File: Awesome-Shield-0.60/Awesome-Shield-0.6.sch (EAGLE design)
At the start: 22 parts, among them SW1 SPST_TACT-EVQQ2, SW2 DPDT, U1 LIGHTSENSORTEMT6000

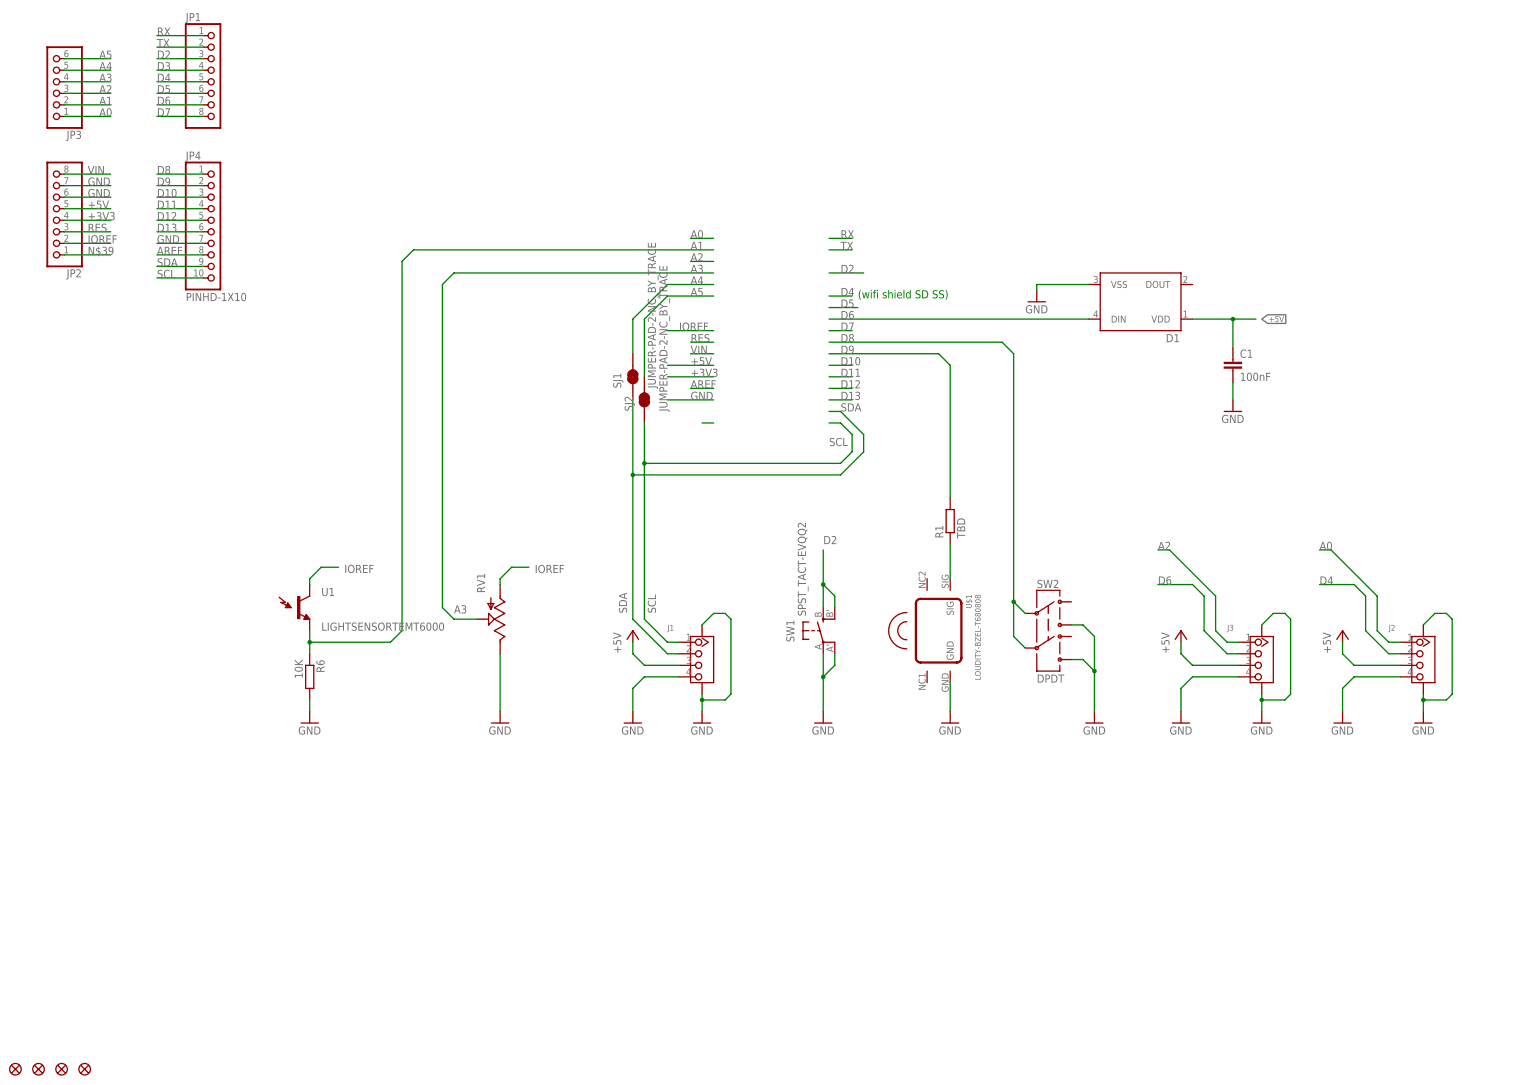
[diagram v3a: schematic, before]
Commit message: LED data to D5 instead of D6
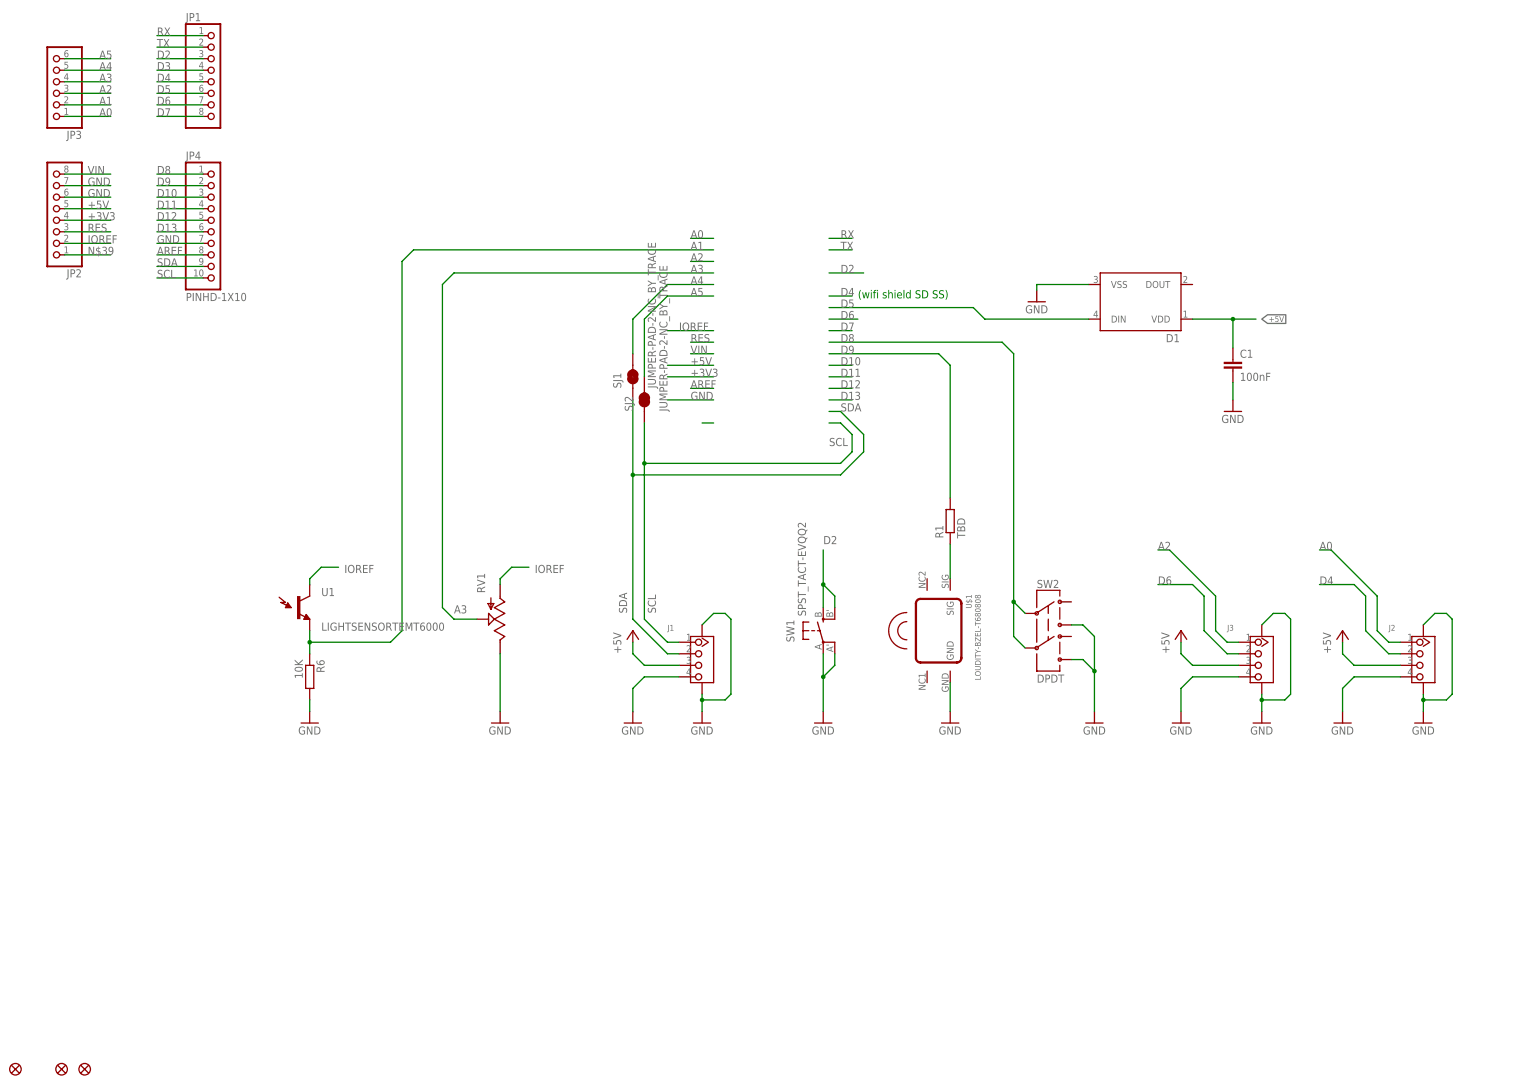
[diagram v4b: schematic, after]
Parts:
- removed FID2: FIDUCIAL1X2, SparkFun-Aesthetics:FIDUCIAL1X2
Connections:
- net D5: now also D1.DIN
- net D6: no longer D1.DIN
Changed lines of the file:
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@@
 <part name="J2" library="Seeed-OPL-Connector" deviceset="GROVE-CONNECTOR-SMD(4+2P-2.0)" device=""/>
 <part name="FID1" library="SparkFun-Aesthetics" deviceset="FIDUCIAL" device="1X2"/>
-<part name="FID2" library="SparkFun-Aesthetics" deviceset="FIDUCIAL" device="1X2"/>
 <part name="FID3" library="SparkFun-Aesthetics" deviceset="FIDUCIAL" device="1X2"/>
 <part name="FID4" library="SparkFun-Aesthetics" deviceset="FIDUCIAL" device="1X2"/>
@@
 <instance part="J2" gate="G$1" x="325.12" y="105.41"/>
 <instance part="FID1" gate="G$1" x="15.24" y="15.24"/>
-<instance part="FID2" gate="G$1" x="20.32" y="15.24"/>
 <instance part="FID3" gate="G$1" x="25.4" y="15.24"/>
 <instance part="FID4" gate="G$1" x="30.48" y="15.24"/>
@@
 <segment>
 <label x="196.85" y="180.34" size="1.778" layer="95"/>
-<pinref part="D1" gate="G$1" pin="DIN"/>
-<wire x1="251.46" y1="180.34" x2="194.31" y2="180.34" width="0.1524" layer="91"/>
+<wire x1="200.66" y1="180.34" x2="194.31" y2="180.34" width="0.1524" layer="91"/>
 </segment>
 <segment>
@@
 <net name="D5" class="0">
 <segment>
-<wire x1="194.31" y1="182.88" x2="200.66" y2="182.88" width="0.1524" layer="91"/>
 <label x="196.85" y="182.88" size="1.778" layer="95"/>
-</segment>
-<segment>
+<pinref part="D1" gate="G$1" pin="DIN"/>
+<wire x1="251.46" y1="180.34" x2="228.6" y2="180.34" width="0.1524" layer="91"/>
+<wire x1="194.31" y1="182.88" x2="226.06" y2="182.88" width="0.1524" layer="91"/>
+<wire x1="226.06" y1="182.88" x2="228.6" y2="180.34" width="0.1524" layer="91"/>
+</segment>
+<segment>

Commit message: routing
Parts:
- J1: value (none) -> PORT1
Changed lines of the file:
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@@
 <part name="RV1" library="SparkFun-Electromechanical" deviceset="POT" device=""/>
 <part name="GND8" library="supply1" deviceset="GND" device=""/>
-<part name="J1" library="Seeed-OPL-Connector" deviceset="GROVE-CONNECTOR-SMD(4+2P-2.0)" device=""/>
+<part name="J1" library="Seeed-OPL-Connector" deviceset="GROVE-CONNECTOR-SMD(4+2P-2.0)" device="" value="PORT1"/>
 <part name="J2" library="Seeed-OPL-Connector" deviceset="GROVE-CONNECTOR-SMD(4+2P-2.0)" device=""/>
 <part name="FID1" library="SparkFun-Aesthetics" deviceset="FIDUCIAL" device="1X2"/>

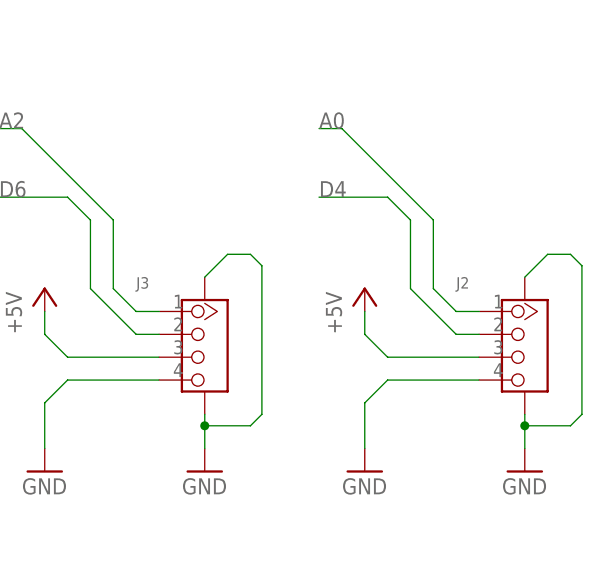
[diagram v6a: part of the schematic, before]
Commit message: added large round silkscreen around LED, solved #31
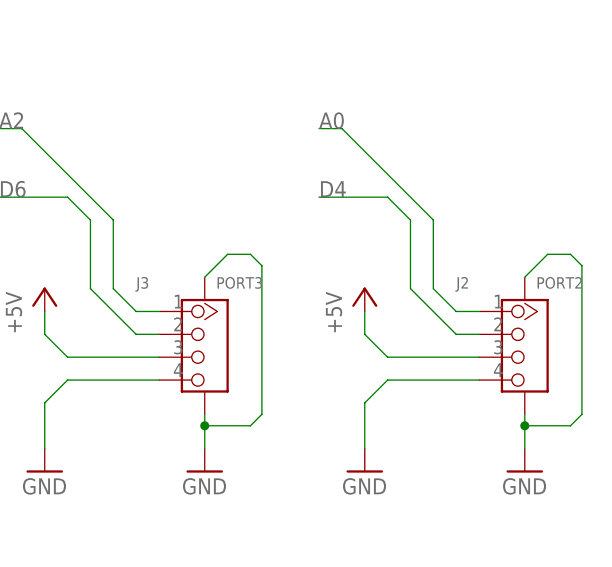
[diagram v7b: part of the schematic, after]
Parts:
- J2: value (none) -> PORT2
- J3: value (none) -> PORT3
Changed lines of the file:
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@@
 <part name="GND8" library="supply1" deviceset="GND" device=""/>
 <part name="J1" library="Seeed-OPL-Connector" deviceset="GROVE-CONNECTOR-SMD(4+2P-2.0)" device="" value="PORT1"/>
-<part name="J2" library="Seeed-OPL-Connector" deviceset="GROVE-CONNECTOR-SMD(4+2P-2.0)" device=""/>
+<part name="J2" library="Seeed-OPL-Connector" deviceset="GROVE-CONNECTOR-SMD(4+2P-2.0)" device="" value="PORT2"/>
 <part name="FID1" library="SparkFun-Aesthetics" deviceset="FIDUCIAL" device="1X2"/>
 <part name="FID3" library="SparkFun-Aesthetics" deviceset="FIDUCIAL" device="1X2"/>
@@
 <part name="P+3" library="supply1" deviceset="+5V" device=""/>
 <part name="GND11" library="supply1" deviceset="GND" device=""/>
-<part name="J3" library="Seeed-OPL-Connector" deviceset="GROVE-CONNECTOR-SMD(4+2P-2.0)" device=""/>
+<part name="J3" library="Seeed-OPL-Connector" deviceset="GROVE-CONNECTOR-SMD(4+2P-2.0)" device="" value="PORT3"/>
 <part name="D1" library="SparkFun-LED" deviceset="WS2812B" device=""/>
 <part name="C1" library="rcl" deviceset="C-EU" device="C0603" value="100nF"/>

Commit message: close #39 close #41 close #42
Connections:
- net D3: now also J2.2
- net D4: no longer J2.2
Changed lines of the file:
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@@
-</segment>
-<segment>
-<wire x1="320.04" y1="106.68" x2="317.5" y2="106.68" width="0.1524" layer="91"/>
-<wire x1="317.5" y1="106.68" x2="312.42" y2="111.76" width="0.1524" layer="91"/>
-<wire x1="312.42" y1="111.76" x2="312.42" y2="119.38" width="0.1524" layer="91"/>
-<wire x1="312.42" y1="119.38" x2="309.88" y2="121.92" width="0.1524" layer="91"/>
-<wire x1="309.88" y1="121.92" x2="302.26" y2="121.92" width="0.1524" layer="91"/>
-<label x="302.26" y="121.92" size="1.778" layer="95"/>
-<pinref part="J2" gate="G$1" pin="2"/>
 </segment>
 <segment>
@@
 <label x="46.38" y="235.12" size="1.778" layer="95"/>
 </segment>
+<segment>
+<wire x1="201.93" y1="187.96" x2="194.31" y2="187.96" width="0.1524" layer="91"/>
+<label x="197.104" y="187.96" size="1.6764" layer="95"/>
+</segment>
+<segment>
+<wire x1="320.04" y1="106.68" x2="317.5" y2="106.68" width="0.1524" layer="91"/>
+<wire x1="317.5" y1="106.68" x2="312.42" y2="111.76" width="0.1524" layer="91"/>
+<wire x1="312.42" y1="111.76" x2="312.42" y2="119.38" width="0.1524" layer="91"/>
+<wire x1="312.42" y1="119.38" x2="309.88" y2="121.92" width="0.1524" layer="91"/>
+<wire x1="309.88" y1="121.92" x2="302.26" y2="121.92" width="0.1524" layer="91"/>
+<label x="302.26" y="121.92" size="1.778" layer="95"/>
+<pinref part="J2" gate="G$1" pin="2"/>
+</segment>
 </net>
